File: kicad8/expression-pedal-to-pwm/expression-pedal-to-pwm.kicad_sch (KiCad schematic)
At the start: 36 parts, among them J4 NMJ6HHD2, J5 Screw_Terminal_01x06, Q1 STP100N8F6, SW1 SW_Push_DPDT, U1 TLV2374, U2 LM7805_TO220

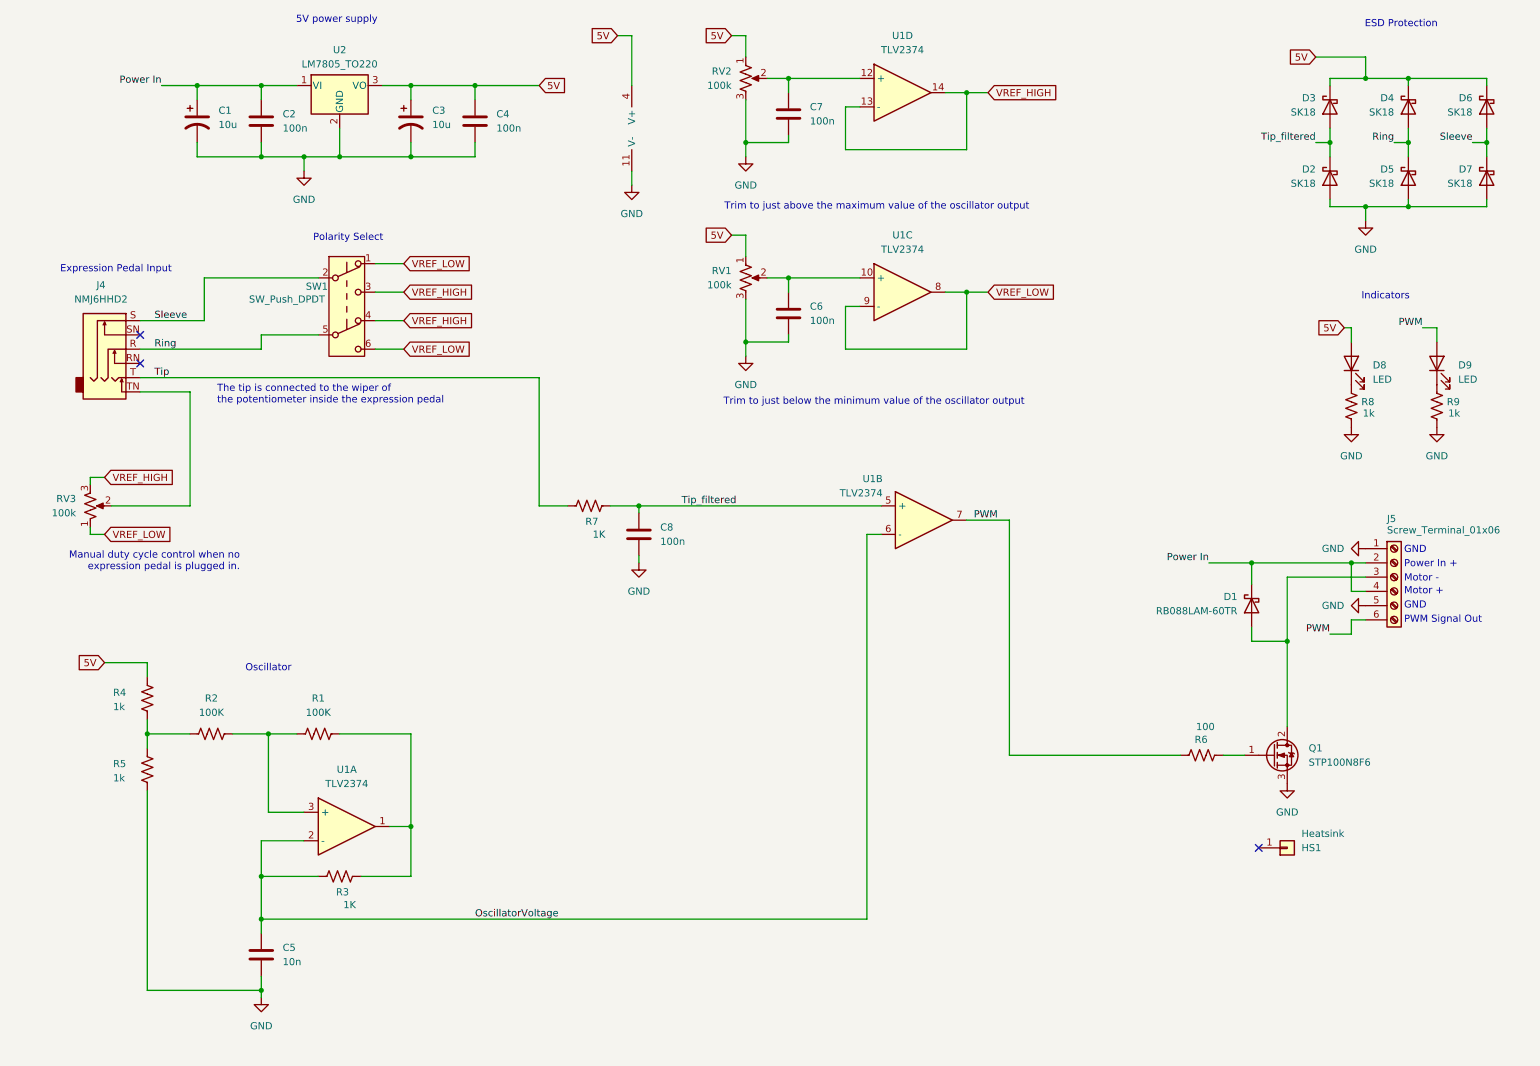
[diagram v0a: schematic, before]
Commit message: Expression-Pedal-to-PWM - make schematic 8.5x11 in
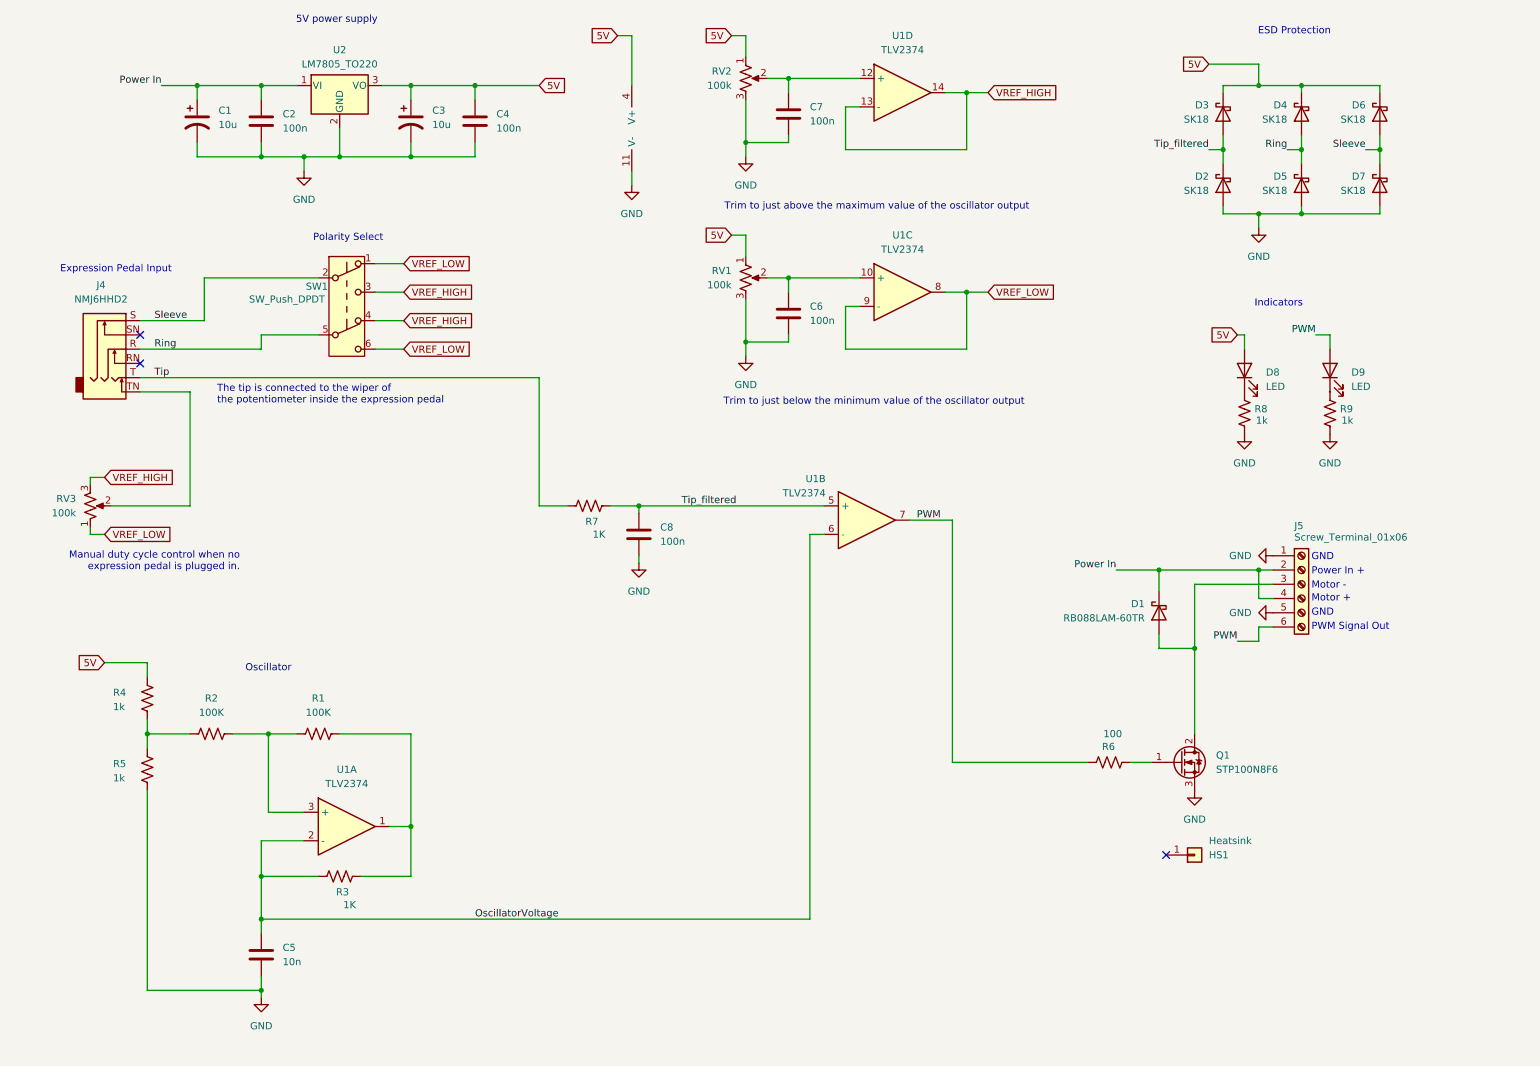
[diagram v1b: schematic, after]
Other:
- title: (none) -> Expression-Pedal-to-PWM
- moved on the sheet: D1, D2, D3, D4, D5, D6, D7, D8, D9, HS1, J5, Q1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

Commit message: Layout components and traces for Expression Pedal PWM Motor Controller
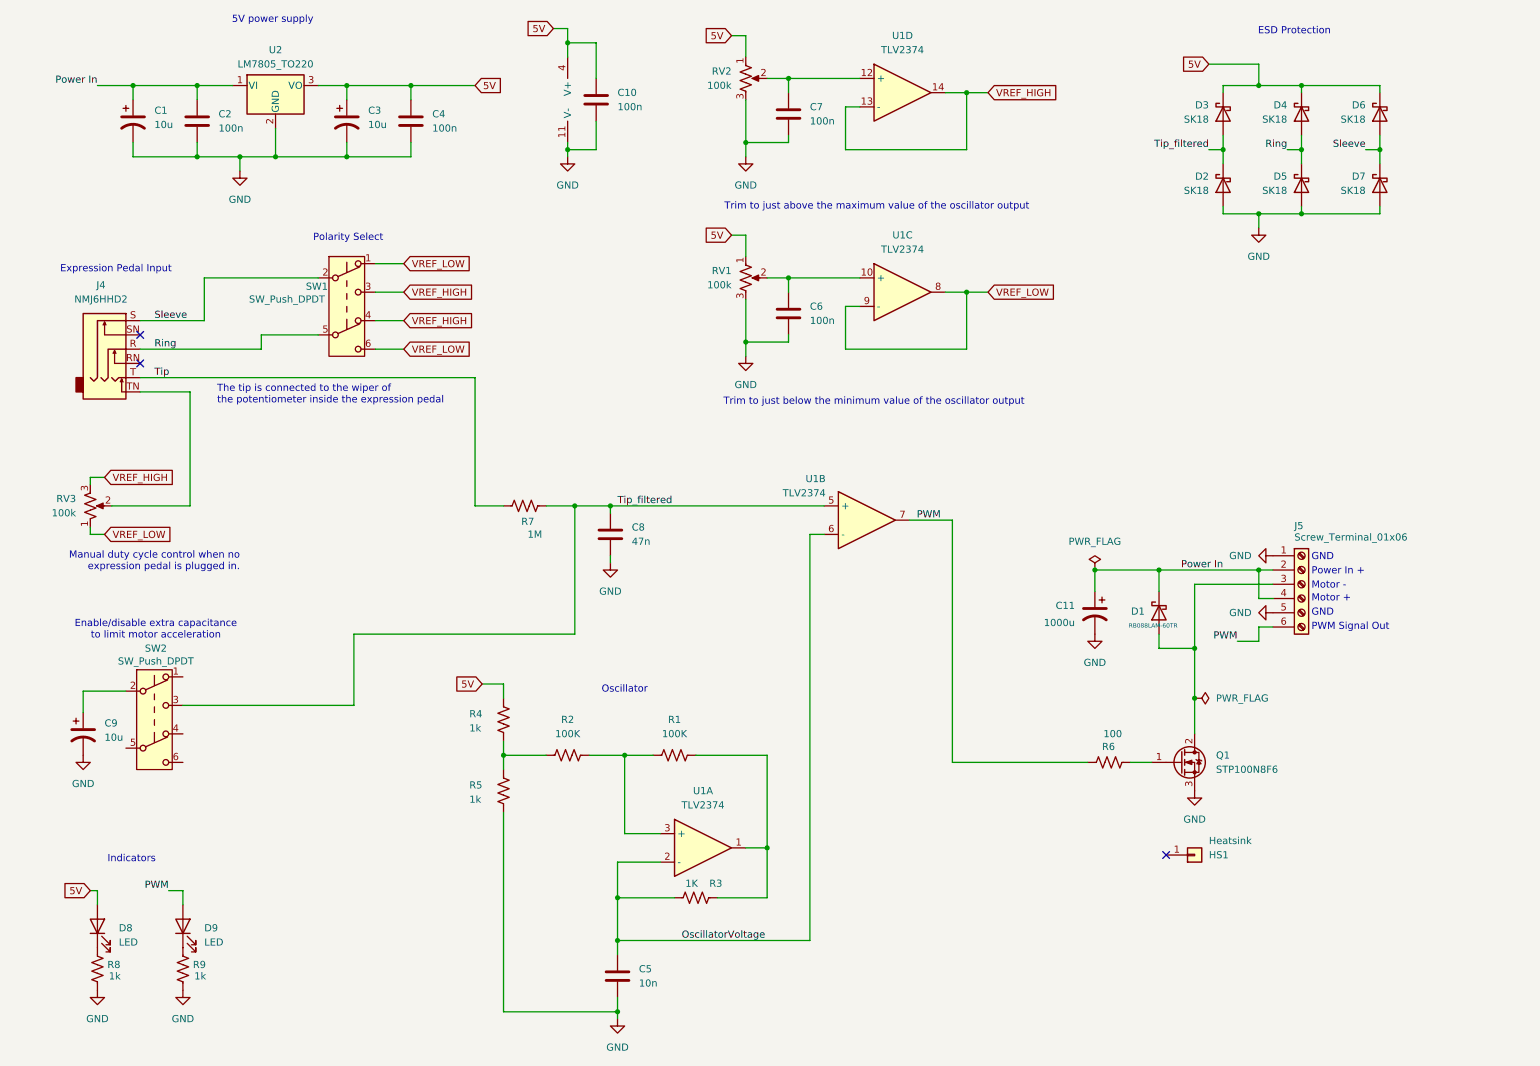
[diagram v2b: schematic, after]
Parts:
- added C10: 100n, Capacitor_SMD:C_0603_1608Metric_Pad1.08x0.95mm_HandSolder, symbol Device:C
- added C11: 1000u, Capacitor_THT:CP_Radial_D10.0mm_P5.00mm, symbol Device:C_Polarized_US
- added C9: 10u, Capacitor_THT:CP_Radial_D5.0mm_P2.50mm, symbol Device:C_Polarized_US
- added SW2: SW_Push_DPDT, Button_Switch_THT:SW_E-Switch_EG2219_DPDT_Angled, symbol Switch:SW_Push_DPDT
- C1, C3: footprint Capacitor_THT:CP_Radial_D10.0mm_P5.00mm -> Capacitor_THT:CP_Radial_D5.0mm_P2.50mm
- C8: value 100n -> 47n
- D8, D9: footprint LED_SMD:LED_1206_3216Metric -> LED_THT:LED_D3.0mm_Horizontal_O3.81mm_Z6.0mm
- R7: value 1K -> 1M
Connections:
- net 5V: now also C10.1
- net GND: now also C10.2, C11.2, C9.2
- net Power In: now also C11.1
- net Tip_filtered: now also SW2.3 (C)
- new net: C9.1, SW2.2 (B)
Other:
- note added: "Enable/disable extra capacitance to limit motor acceleration"
- moved on the sheet: C1, C2, C3, C4, C5, C8, D8, D9, R1, R2, R3, R4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
